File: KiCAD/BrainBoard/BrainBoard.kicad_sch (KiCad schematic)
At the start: 2 parts, among them J1 Battery Input

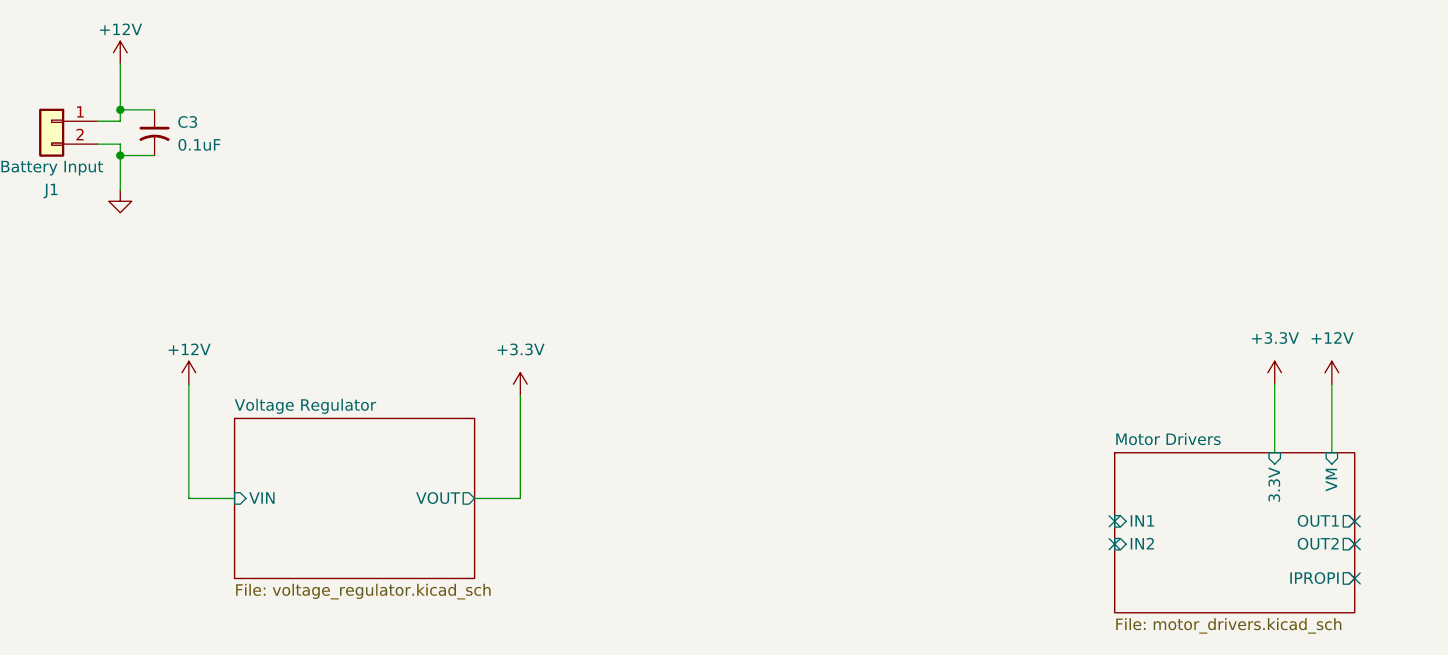
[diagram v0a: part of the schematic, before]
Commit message: [feature] Finalize DRV8231DSGR motor drivers
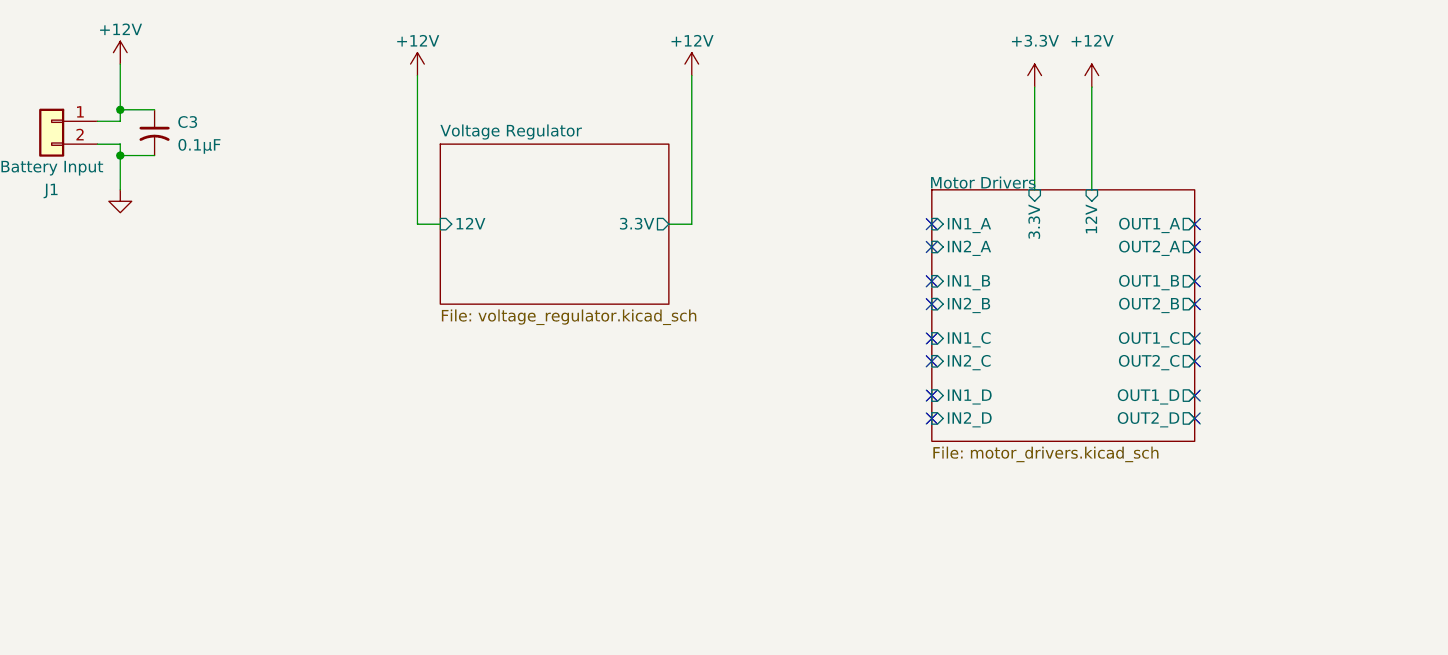
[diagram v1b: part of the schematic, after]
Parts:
- C3: value 0.1uF -> 0.1µF
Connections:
- no-connect marks 5 -> 16
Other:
- sheet Motor Drivers ports: added 12V, IN1_A, IN1_B, IN1_C, IN1_D, IN2_A, IN2_B, IN2_C, IN2_D, OUT1_A, OUT1_B, OUT1_C, OUT1_D, OUT2_A, OUT2_B, OUT2_C, OUT2_D; removed IN1, IN2, IPROPI, OUT1, OUT2, VM
- sheet Voltage Regulator ports: added 12V, 3.3V; removed VIN, VOUT
- company: Nathan Wignall, Minh Nguyen, Ana Weiss -> Nathan Wignall, Minh Nguyen, Ana Wise

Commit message: feat: Processor add
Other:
- added sheet STM32F303CCT6 Microcontroller (Microcontroller.kicad_sch)
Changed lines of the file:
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@@
+		)
+	)
+	(sheet
+		(at 196.85 93.98)
+		(size 27.94 53.34)
+		(exclude_from_sim no)
+		(in_bom yes)
+		(on_board yes)
+		(dnp no)
+		(fields_autoplaced yes)
+		(stroke
+			(width 0.1524)
+			(type solid)
+		)
+		(fill
+			(color 0 0 0 0.0000)
+		)
+		(property "Sheetname" "STM32F303CCT6 Microcontroller"
+			(at 196.85 93.2684 0)
+			(effects
+				(font
+					(size 1.27 1.27)
+				)
+				(justify left bottom)
+			)
+		)
+		(property "Sheetfile" "Microcontroller.kicad_sch"
+			(at 196.85 147.9046 0)
+			(effects
+				(font
+					(size 1.27 1.27)
+				)
+				(justify left top)
+			)
+		)
+		(instances
+			(project "BrainBoard"
+				(path "/44e391a9-9312-4881-bf0a-d93a44472e34"
+					(page "4")
+				)
+			)
 		)
 	)

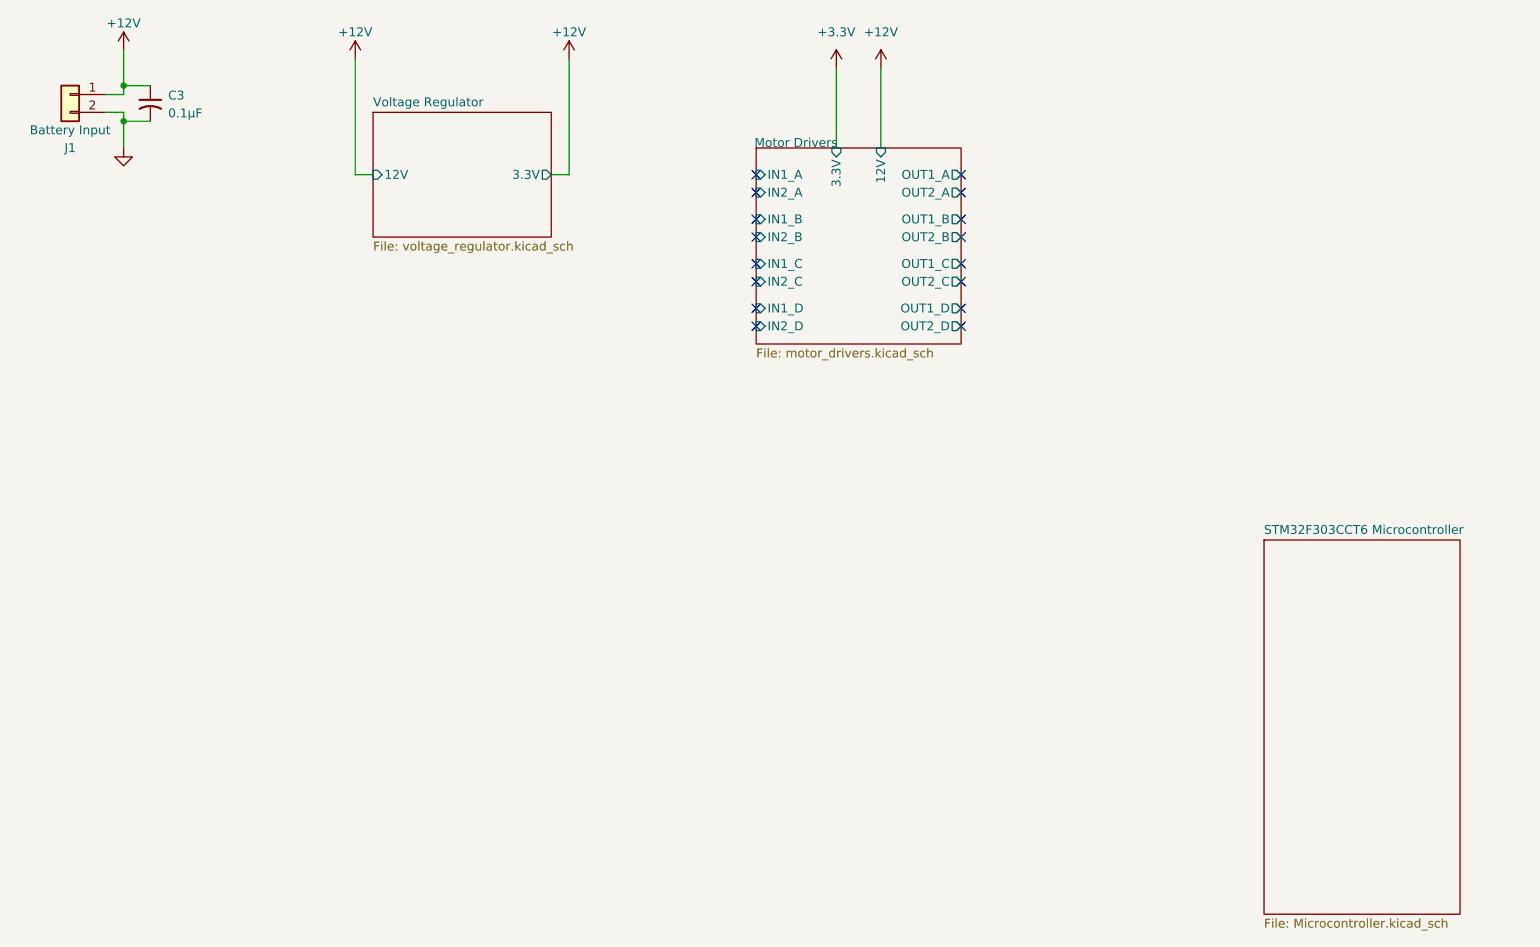
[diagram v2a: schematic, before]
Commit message: fix: Make DRC happy
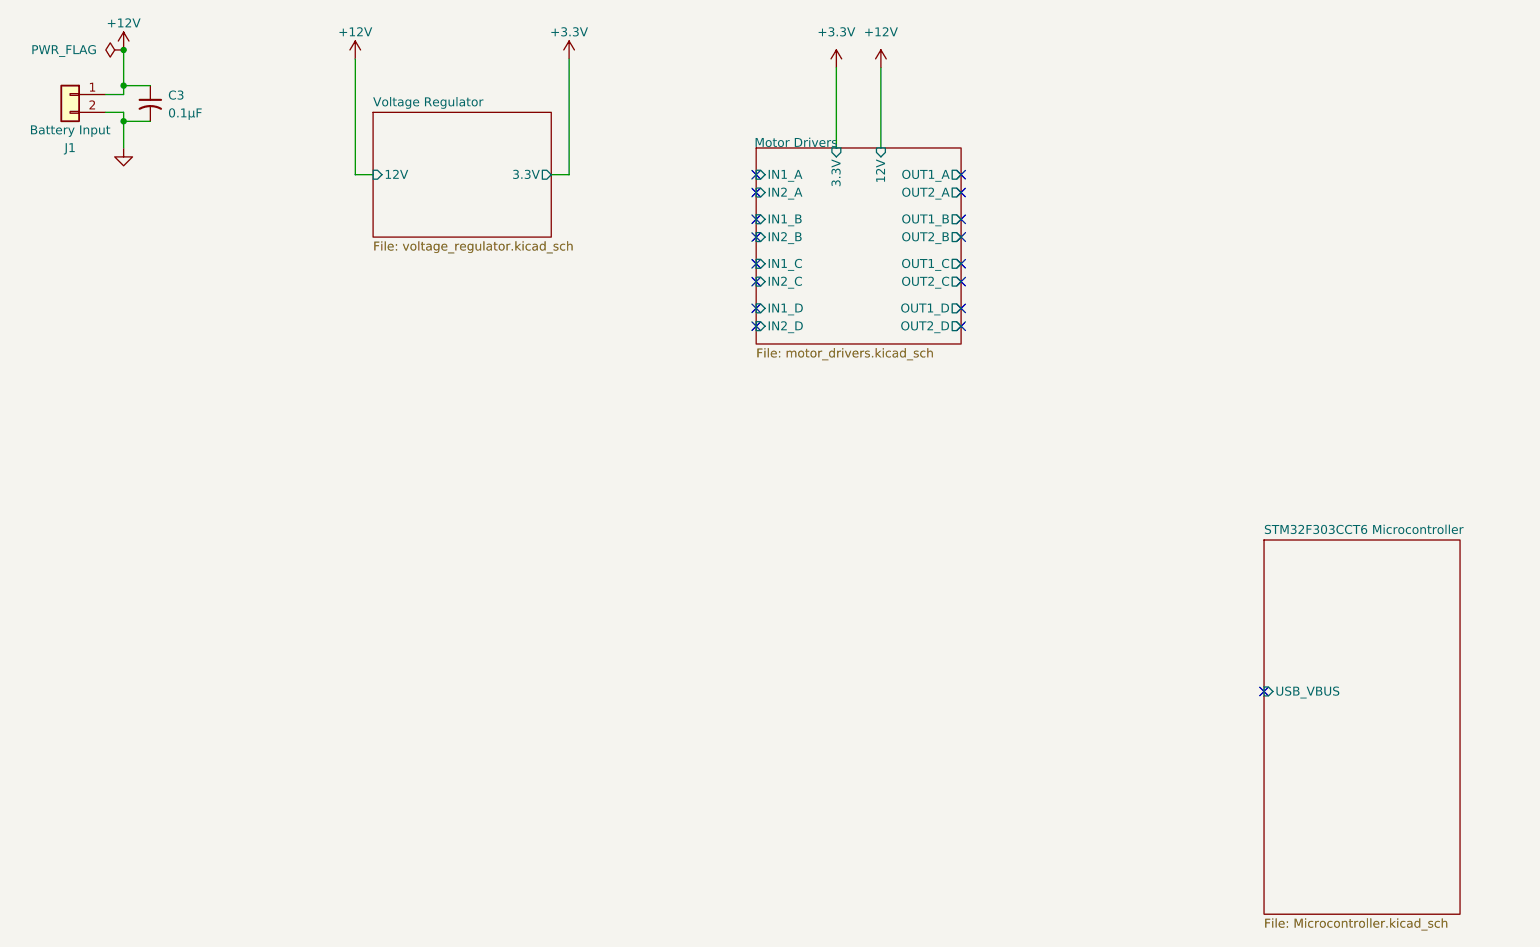
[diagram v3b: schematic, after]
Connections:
- no-connect marks 16 -> 17
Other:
- sheet STM32F303CCT6 Microcontroller ports: added USB_VBUS; removed none
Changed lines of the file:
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@@
+	)
+	(junction
+		(at 34.29 24.13)
+		(diameter 0)
+		(color 0 0 0 0)
 	)
 	(junction
@@
 	)
 	(no_connect
+		(at 196.85 115.57)
+	)
+	(no_connect
 		(at 124.46 60.96)
 	)
@@
 	(wire
 		(pts
+			(xy 34.29 33.02) (xy 34.29 34.29)
+		)
+		(stroke
+			(width 0)
+			(type default)
+		)
+	)
+	(wire
+		(pts
+			(xy 34.29 29.21) (xy 38.1 29.21)
+		)
+		(stroke
+			(width 0)
+			(type default)
+		)
+	)
+	(wire
+		(pts
+			(xy 67.31 25.4) (xy 67.31 41.91)
+		)
+		(stroke
+			(width 0)
+			(type default)
+		)
+	)
+	(wire
+		(pts
+			(xy 135.89 26.67) (xy 135.89 38.1)
+		)
+		(stroke
+			(width 0)
+			(type default)
+		)
+	)
+	(wire
+		(pts
+			(xy 34.29 30.48) (xy 31.75 30.48)
+		)
+		(stroke
+			(width 0)
+			(type default)
+		)
+	)
+	(wire
+		(pts
+			(xy 34.29 33.02) (xy 31.75 33.02)
+		)
+		(stroke
+			(width 0)
+			(type default)
+		)
+	)
+	(wire
+		(pts
+			(xy 34.29 34.29) (xy 38.1 34.29)
+		)
+		(stroke
+			(width 0)
+			(type default)
+		)
+	)
+	(wire
+		(pts
 			(xy 34.29 24.13) (xy 34.29 29.21)
-		)
-		(stroke
-			(width 0)
-			(type default)
-		)
-	)
-	(wire
-		(pts
-			(xy 34.29 33.02) (xy 34.29 34.29)
-		)
-		(stroke
-			(width 0)
-			(type default)
-		)
-	)
-	(wire
-		(pts
-			(xy 34.29 29.21) (xy 38.1 29.21)
-		)
-		(stroke
-			(width 0)
-			(type default)
-		)
-	)
-	(wire
-		(pts
-			(xy 67.31 25.4) (xy 67.31 41.91)
-		)
-		(stroke
-			(width 0)
-			(type default)
-		)
-	)
-	(wire
-		(pts
-			(xy 135.89 26.67) (xy 135.89 38.1)
-		)
-		(stroke
-			(width 0)
-			(type default)
-		)
-	)
-	(wire
-		(pts
-			(xy 34.29 30.48) (xy 31.75 30.48)
-		)
-		(stroke
-			(width 0)
-			(type default)
-		)
-	)
-	(wire
-		(pts
-			(xy 34.29 33.02) (xy 31.75 33.02)
-		)
-		(stroke
-			(width 0)
-			(type default)
-		)
-	)
-	(wire
-		(pts
-			(xy 34.29 34.29) (xy 38.1 34.29)
 		)
 		(stroke
@@
 	)
 	(symbol
+		(lib_id "power:PWR_FLAG")
+		(at 34.29 24.13 90)
+		(unit 1)
+		(exclude_from_sim no)
+		(in_bom yes)
+		(on_board yes)
+		(dnp no)
+		(fields_autoplaced yes)
+		(property "Reference" "#FLG03"
+			(at 32.385 24.13 0)
+			(effects
+				(font
+					(size 1.27 1.27)
+				)
+				(hide yes)
+			)
+		)
+		(property "Value" "PWR_FLAG"
+			(at 30.48 24.1299 90)
+			(effects
+				(font
+					(size 1.27 1.27)
+				)
+				(justify left)
+			)
+		)
+		(property "Footprint" ""
+			(at 34.29 24.13 0)
+			(effects
+				(font
+					(size 1.27 1.27)
+				)
+				(hide yes)
+			)
+		)
+		(property "Datasheet" "~"
+			(at 34.29 24.13 0)
+			(effects
+				(font
+					(size 1.27 1.27)
+				)
+				(hide yes)
+			)
+		)
+		(property "Description" "Special symbol for telling ERC where power comes from"
+			(at 34.29 24.13 0)
+			(effects
+				(font
+					(size 1.27 1.27)
+				)
+				(hide yes)
+			)
+		)
+		(pin "1"
+		)
+		(instances
+			(project "BrainBoard"
+				(path "/44e391a9-9312-4881-bf0a-d93a44472e34"
+					(reference "#FLG03")
+					(unit 1)
+				)
+			)
+		)
+	)
+	(symbol
 		(lib_id "power:+12V")
 		(at 97.79 25.4 0)
@@
 			)
 		)
-		(property "Value" "+12V"
+		(property "Value" "+3.3V"
 			(at 97.79 21.59 0)
 			(effects
@@
 			)
 		)
+		(pin "USB_VBUS" input
+			(at 196.85 115.57 180)
+			(effects
+				(font
+					(size 1.27 1.27)
+				)
+				(justify left)
+			)
+		)
